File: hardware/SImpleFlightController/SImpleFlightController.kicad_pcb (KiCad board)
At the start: 2 copper layers, 50 x 50 mm, 79 parts, among them J1 Screw_Terminal_01x02, J2 Conn_01x03, J3 Conn_01x03, SW1 TS-1088-AR02016, SW2 TS-1088-AR02016, U1 BQ25883RGER, U2 ICM-45686, U3 STM32F722RETx, U4 BMP580, U5 TPS63070RNMR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

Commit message: added local files
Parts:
- added G***: LOGO, LOGO, F.Cu at (149.3, 61.6)
- added G***: LOGO, LOGO, B.Cu at (165.9, 84.6)
- moved J1 0.70 mm to (187.2, 92.1)
- turned D1 to 90 degrees
- renumbered SW2 to BOOT, SW1 to RESET
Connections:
- R7 pad 1: Net-(D1-A) -> Net-(D1-K)
- U1 pad 2: Net-(D1-K) -> Net-(D1-A)
- U1 pad 25: unconnected-(U1-EP-Pad25) -> GND
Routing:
- net +3V3: track 2.19 -> 177.7 mm, vias 0 -> 4
- net GND: track 0.00 -> 71.0 mm, vias 0 -> 17
- net /SERVO1: track 0.00 -> 55.1 mm, vias 0 -> 2
- net /SERVO2: track 0.00 -> 50.8 mm, vias 0 -> 2
- net PGND: track 0.00 -> 30.0 mm, vias 0 -> 2
- net /SD_CD: track 0.00 -> 25.8 mm, vias 0 -> 2
- net /RESET: track 0.00 -> 20.7 mm, vias 0 -> 2
- net VSYS: track 15.2 -> 34.7 mm
- net /BOOT: track 0.00 -> 17.9 mm, vias 0 -> 2
- net /HSE_IN: track 0.00 -> 10.8 mm
- net /ICM_INT2: track 7.42 -> 17.4 mm, vias 0 -> 2
- net /ICM_INT1: track 12.1 -> 21.6 mm
- net Net-(U6-SW): track 0.00 -> 9.10 mm
- net /HSE_OUT: track 0.00 -> 8.93 mm
- net /LSE_OUT: track 0.00 -> 8.26 mm
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- added copper zone on B.Cu, net GND
- added copper zone on F.Cu, net GND
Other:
- board text added: "+"
- board text added: "-"
- board text added: "Arwin Silpakar"

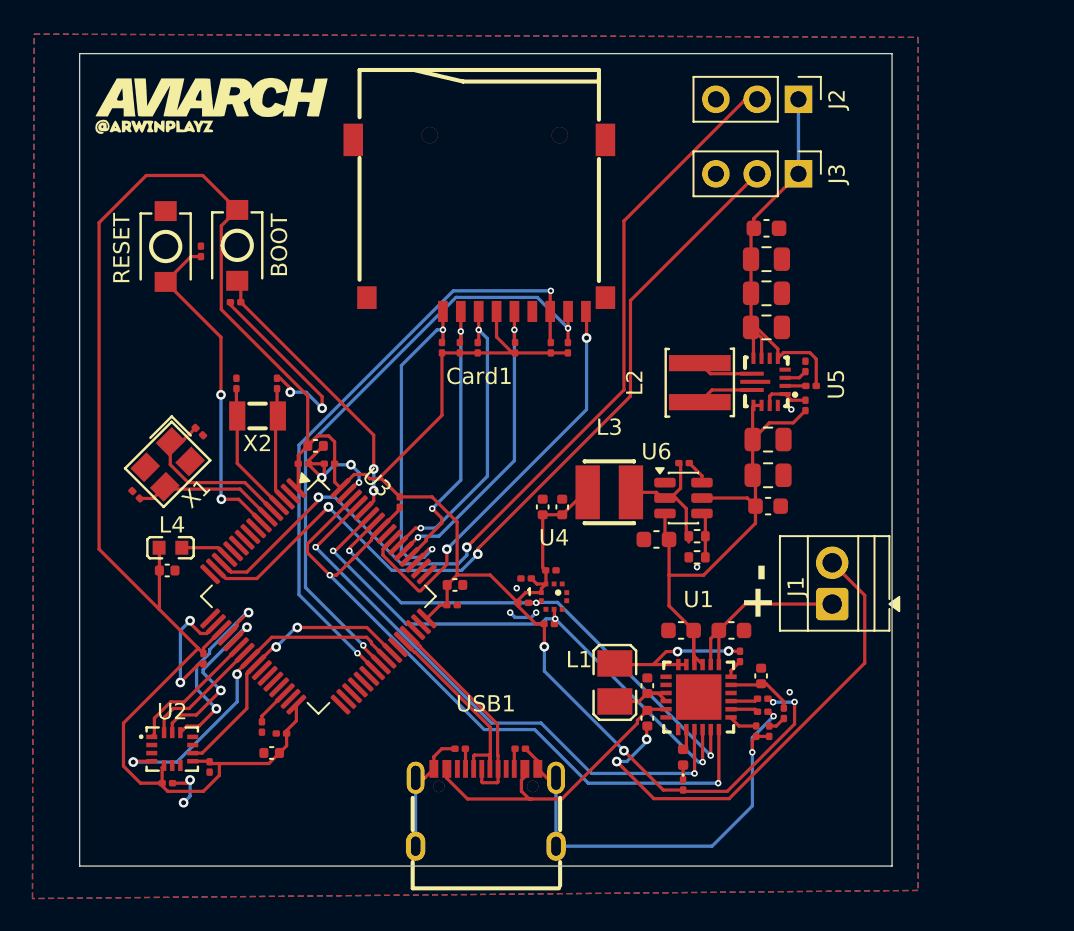
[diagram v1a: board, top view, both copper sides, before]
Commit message: updated GPS to front
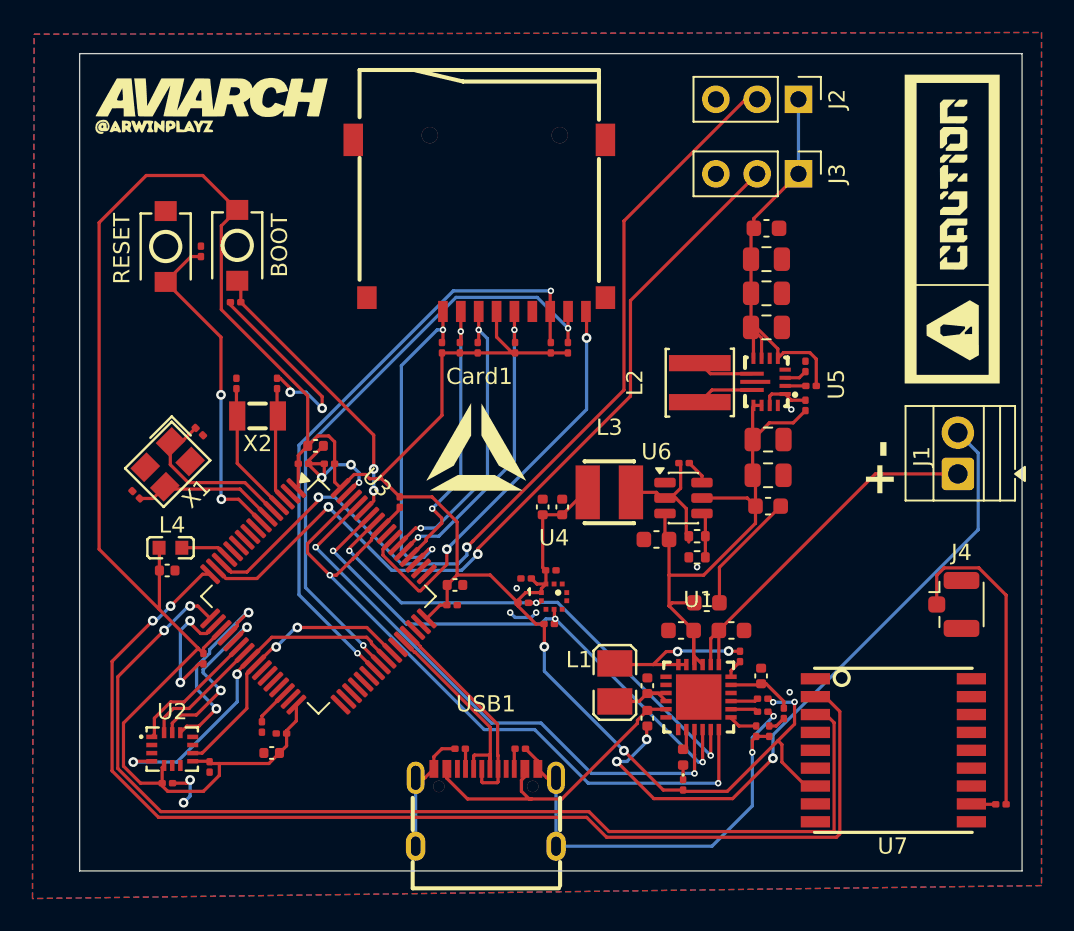
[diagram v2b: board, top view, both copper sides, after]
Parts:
- removed the G*** at (165.9, 84.6)
- added C38: 22uF, Capacitor_SMD:C_0603_1608Metric, F.Cu at (179.5, 92.0)
- added G***: LOGO, LOGO, F.Cu at (194.6, 69.0)
- added G***: LOGO, LOGO, F.Cu at (165.3, 82.5)
- added G***: LOGO, LOGO, B.Cu at (168.8, 82.0)
- added G***: LOGO, LOGO, B.Cu at (151.6, 105.1)
- added G***: LOGO, LOGO, B.Cu at (167.2, 61.6)
- added G***: LOGO, LOGO, B.Cu at (195.9, 83.2)
- added J4: Conn_Coaxial, Connector_Coaxial:U.FL_Hirose_U.FL-R-SMT-1_Vertical, F.Cu at (194.7, 92.1)
- added R23: 0, Resistor_SMD:R_0201_0603Metric, F.Cu at (197.6, 104.4)
- added U7: MAX-M10S-00B, lcsc:SMD-18_L10.1-W9.7-P1.10-TL_SKG09F, F.Cu at (191.0, 101.1)
- C6: value 44uF -> 22uF
- moved J1 11.1 mm to (194.9, 84.1)
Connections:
- U1 pad 25: GND -> unconnected-(U1-EP-Pad25)
- U3 pad 16: unconnected-(U3-PA2-Pad16) -> /GPS_TX
- U3 pad 17: unconnected-(U3-PA3-Pad17) -> /GPS_RX
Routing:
- net /GPS_TX: track 0.00 -> 71.0 mm, vias 0 -> 2
- net /GPS_RX: track 0.00 -> 67.2 mm, vias 0 -> 2
- net Net-(J4-In): track 0.00 -> 19.8 mm
- net BAT+: track 12.1 -> 23.1 mm
- net PGND: track 30.0 -> 40.7 mm, vias 2 -> 3
- net GND: track 71.0 -> 78.5 mm
- net +3V3: track 177.7 -> 182.3 mm
- net Net-(U7-RF_IN): track 0.00 -> 1.79 mm
- net VSYS: track 34.7 -> 36.3 mm
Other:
- board size 50 x 50 mm -> 58 x 50.3 mm
- board text removed: "Arwin Silpakar"
